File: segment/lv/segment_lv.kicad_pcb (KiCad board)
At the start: 2 copper layers, 49.5 x 63.5 mm, 10 parts, among them J1 Thermistors In [1-12], J2 Thermistors In [13-24], J3 Thermistors Out [1-12], J4 Thermistors Out [13-24]

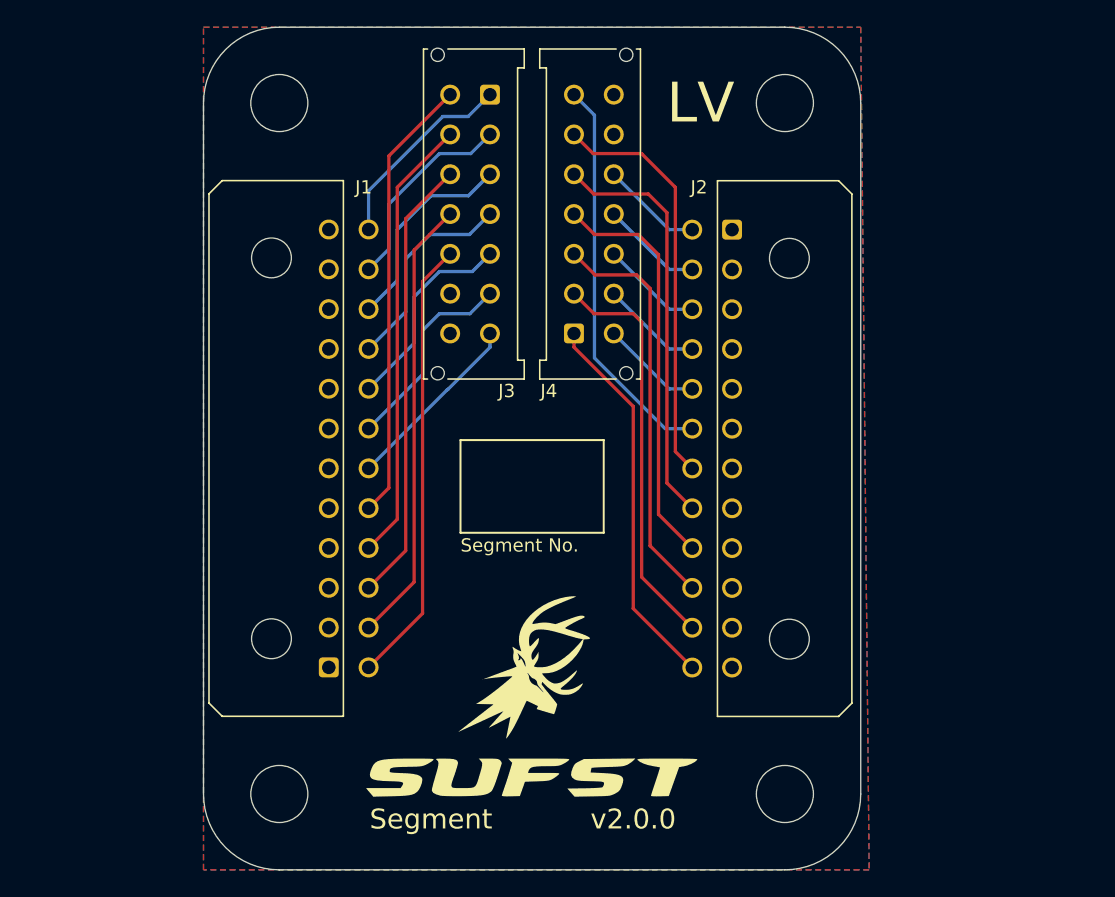
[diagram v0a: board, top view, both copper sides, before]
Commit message: feat(segment): reduce size of LV board
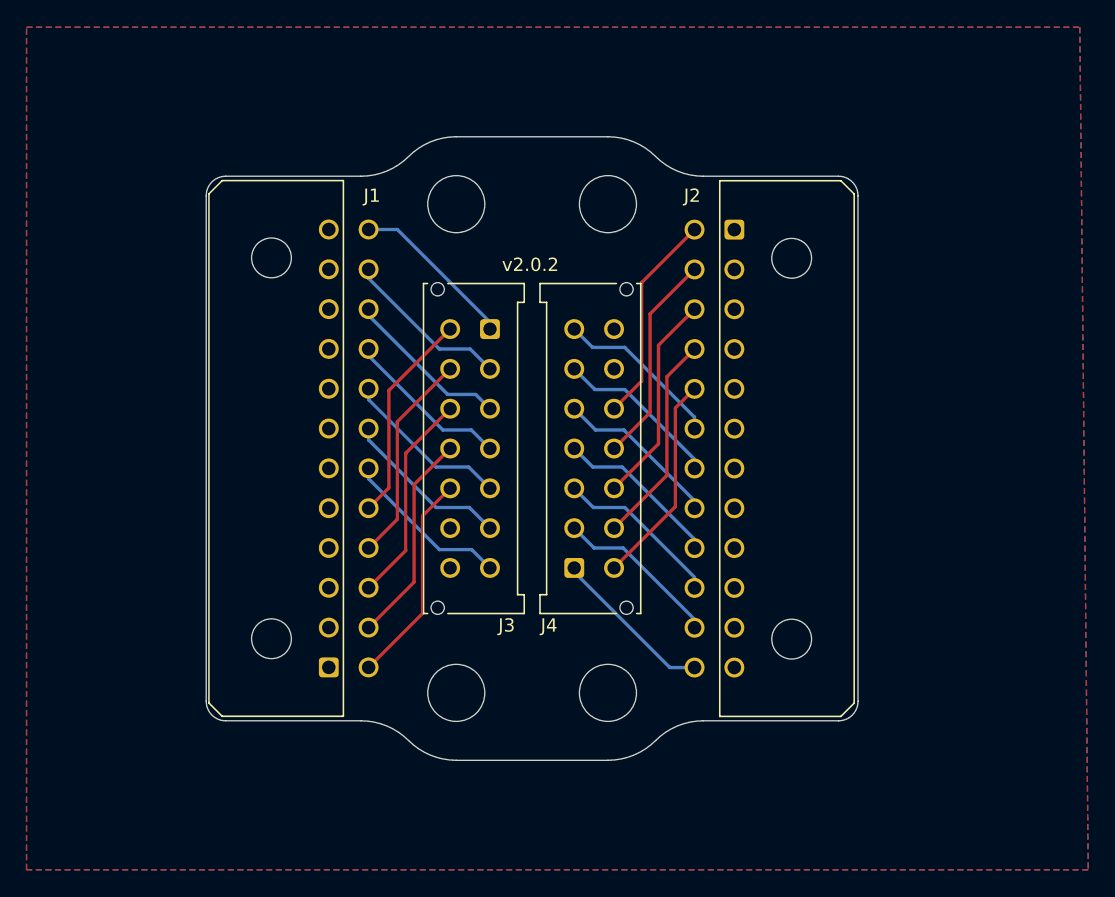
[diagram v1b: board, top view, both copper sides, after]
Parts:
- removed the G*** at (147.3, 108.6)
- removed the G*** at (148.0, 116.8)
- added G***: LOGO, LOGO, B.Cu at (167.1, 92.1)
- moved J4 17.7 mm to (151.1, 101.1)
- moved J3 17.7 mm to (144.8, 83.1)
- moved H1 15.4 mm to (153.7, 110.5)
- moved H4 15.4 mm to (142.2, 110.5)
- moved H2 15.4 mm to (153.7, 73.7)
- moved H3 15.4 mm to (142.2, 73.7)
- moved J2 0.17 mm to (163.2, 75.6)
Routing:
- net /THERM_17: track 31.3 -> 12.5 mm
- net /THERM_18: track 31.0 -> 12.6 mm
- net /THERM_16: track 30.8 -> 12.6 mm
- net /THERM_15: track 30.7 -> 12.6 mm
- net /THERM_14: track 30.6 -> 12.5 mm
- net /THERM_9: track 33.7 -> 16.0 mm
- net /THERM_12: track 33.7 -> 16.0 mm
- net /THERM_11: track 33.7 -> 16.0 mm
- net /THERM_10: track 33.7 -> 16.0 mm
- net /THERM_8: track 33.7 -> 16.0 mm
- net /THERM_19: track 30.1 -> 12.7 mm
- net /THERM_13: track 28.9 -> 12.3 mm
- net /THERM_24: track 7.64 -> 16.0 mm
- net /THERM_21: track 7.64 -> 16.0 mm
- net /THERM_23: track 7.64 -> 16.0 mm
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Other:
- board size 49.5 x 63.5 mm -> 49.1 x 47 mm
- board text added: "v2.0.2"
- board text removed: "Segment No."
- board text removed: "Segment will be wired such that voltage taps of increasing number have increasing voltage Routing has been done carefully to minimise the voltage between traces which are close to each other The maximum voltage between any two traces on this board is approx 50V All tracks have a minimum clearance of 0.5mm from pads and other tracks The {dblquote}worst case{dblquote} clearance is where voltage tap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"
- board text removed: "Thermistors"
- board text removed: "v2.0.0"
